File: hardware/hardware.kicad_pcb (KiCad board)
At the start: 2 copper layers, 25.7 x 34.4 mm, 10 parts, among them P1 CONN_01X08, P2 CONN_01X08, P3 CONN_01X02

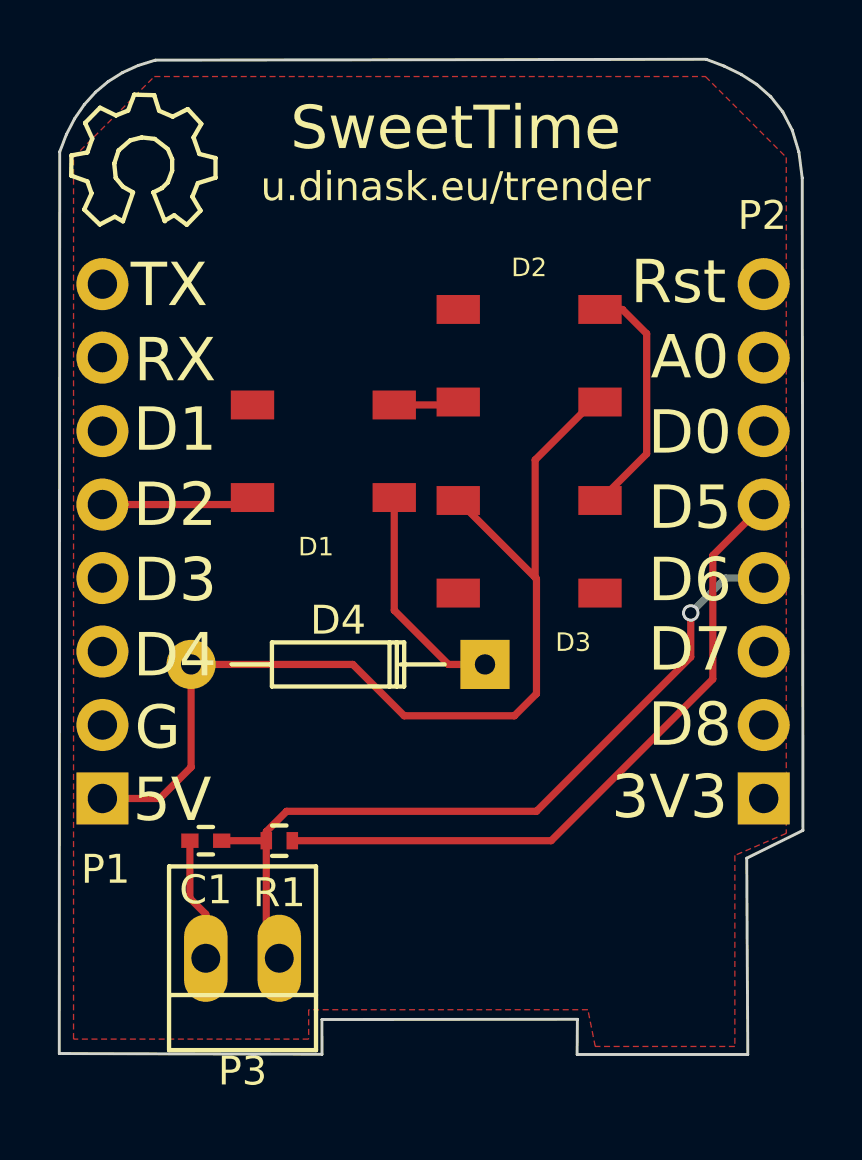
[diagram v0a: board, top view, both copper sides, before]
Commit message: 1st re-reading * serial resistor with DIN * decoupling capa for led power * D4 footprint
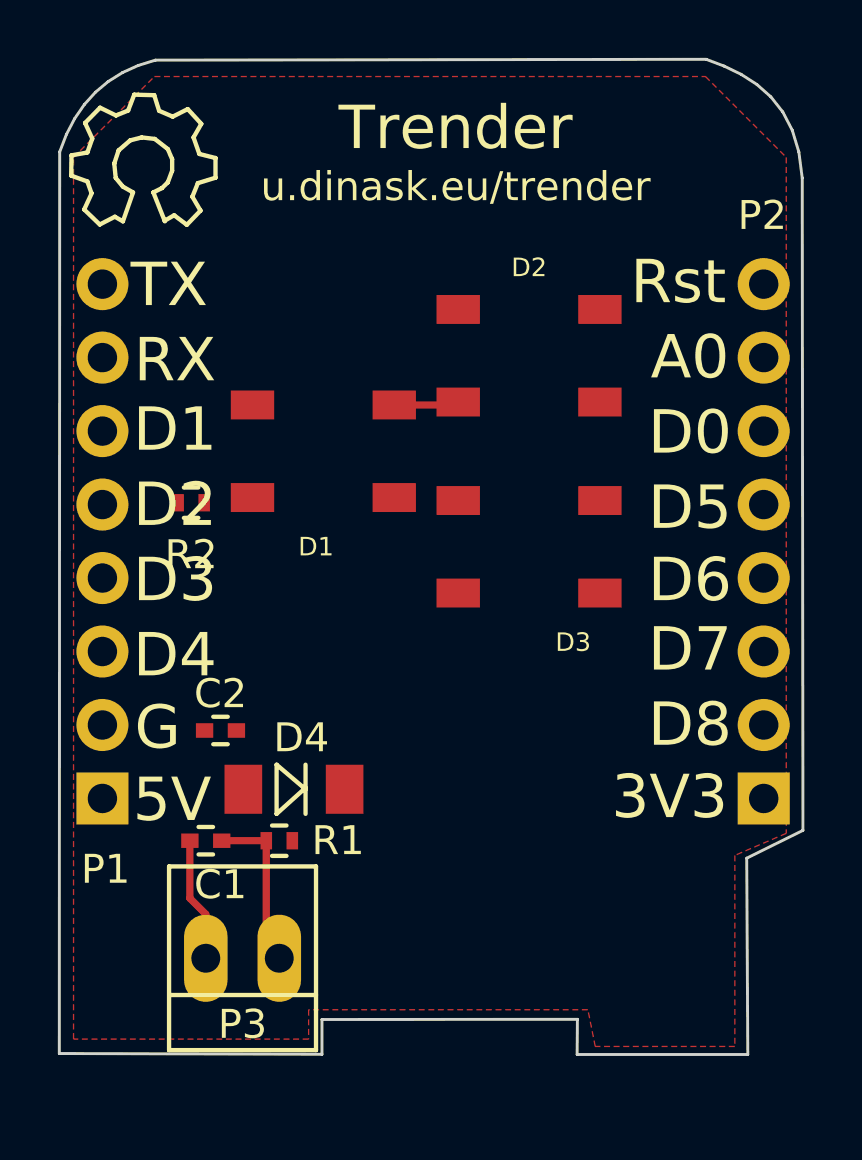
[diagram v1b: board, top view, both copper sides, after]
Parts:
- added C2: 4.7u, Capacitors_SMD:C_0402, F.Cu at (131.6, 101.6)
- added R2: 470, Resistors_SMD:R_0402, F.Cu at (130.6, 93.7)
- D4: value 1N4004 -> 1N4148; footprint Diodes_ThroughHole:Diode_DO-35_SOD27_Horizontal_RM10 -> Diodes_SMD:MiniMELF_Standard
- moved D4 7.89 mm to (134.1, 103.6)
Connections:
- D1 pad 4: /D2 -> Net-(D1-Pad4)
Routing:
- net /+5V: track 35.0 -> 0.24 mm
- net /D5: track 23.6 -> 0.00 mm
- net /D6: track 27.8 -> 5.79 mm, vias 1 -> 0
- net Net-(D2-Pad2): track 8.40 -> 0.00 mm
- net Net-(D1-Pad1): track 7.81 -> 0.00 mm
- net /D2: track 5.29 -> 0.00 mm
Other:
- board text added: "Trender"
- board text removed: "SweetTime"

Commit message: 1st review : placement/routage
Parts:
- moved C2 7.22 mm to (136.1, 96.0)
- moved D4 4.50 mm to (132.8, 99.3), turned to 270 degrees
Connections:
- C1 pad 1: /D6 -> /D5
- P3 pad 1: /D6 -> /D5
- R1 pad 1: /D5 -> /D6
- R1 pad 2: /D6 -> /D5
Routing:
- net /D5: track 0.00 -> 29.2 mm
- net /+5V: track 0.24 -> 24.0 mm
- net /D6: track 5.79 -> 20.1 mm
- net Net-(D2-Pad2): track 0.00 -> 7.74 mm
- net Net-(D1-Pad1): track 0.00 -> 6.85 mm
- net /D2: track 0.00 -> 2.64 mm
- net Net-(D1-Pad4): track 0.34 -> 2.09 mm
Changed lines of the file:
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@@
   (general
     (links 19)
-    (no_connects 11)
+    (no_connects 0)
     (area 125.949806 78.348265 151.756027 112.850001)
     (thickness 1.6)
     (drawings 75)
-    (tracks 11)
+    (tracks 44)
     (zones 0)
     (modules 12)
@@
     (34 B.Paste user)
     (35 F.Paste user)
-    (36 B.SilkS user)
+    (36 B.SilkS user hide)
     (37 F.SilkS user)
     (38 B.Mask user)
@@
     (fp_line (start -0.25 0.475) (end 0.25 0.475) (layer F.SilkS) (width 0.15))
     (pad 1 smd rect (at -0.55 0 180) (size 0.6 0.5) (layers F.Cu F.Paste F.Mask)
-      (net 11 /D6))
+      (net 12 /D5))
     (pad 2 smd rect (at 0.55 0 180) (size 0.6 0.5) (layers F.Cu F.Paste F.Mask)
       (net 16 GND))
@@
     (fp_line (start 2.54 -3.175) (end 2.54 3.175) (layer F.SilkS) (width 0.15))
     (pad 1 thru_hole oval (at -1.27 0 180) (size 1.50622 3.01498) (drill 0.99822) (layers *.Cu *.Mask)
-      (net 11 /D6))
+      (net 12 /D5))
     (pad 2 thru_hole oval (at 1.27 0 180) (size 1.50622 3.01498) (drill 0.99822) (layers *.Cu *.Mask)
       (net 16 GND))
@@
     (fp_line (start -0.25 0.525) (end 0.25 0.525) (layer F.SilkS) (width 0.15))
     (pad 1 smd rect (at -0.45 0 180) (size 0.4 0.6) (layers F.Cu F.Paste F.Mask)
+      (net 11 /D6))
+    (pad 2 smd rect (at 0.45 0 180) (size 0.4 0.6) (layers F.Cu F.Paste F.Mask)
       (net 12 /D5))
-    (pad 2 smd rect (at 0.45 0 180) (size 0.4 0.6) (layers F.Cu F.Paste F.Mask)
-      (net 11 /D6))
     (model Resistors_SMD.3dshapes/R_0402.wrl
       (at (xyz 0 0 0))
@@
   )
   (module Capacitors_SMD:C_0402 (layer F.Cu)
-    (at 131.572 101.6 180)
+    (at 136.144 96.012 180)
     (descr "Capacitor SMD 0402, reflow soldering, AVX (see smccp.pdf)")
     (tags "capacitor 0402")
     (attr smd)
-    (fp_text reference C2 (at 0 1.27 180) (layer F.SilkS)
+    (fp_text reference C2 (at 0 -1.27 180) (layer F.SilkS)
       (effects (font (size 1 1) (thickness 0.15)))
     )
@@
   )
   (module Diodes_SMD:MiniMELF_Standard (layer F.Cu)
-    (at 134.112 103.632 180)
+    (at 132.842 99.314 270)
     (descr "Diode Mini-MELF Standard")
     (tags "Diode Mini-MELF Standard")
     (attr smd)
-    (fp_text reference D4 (at -0.254 1.778 180) (layer F.SilkS)
-      (effects (font (size 1 1) (thickness 0.15)))
-    )
-    (fp_text value 1N4148 (at 0 3.81 180) (layer F.Fab) hide
+    (fp_text reference D4 (at 0 -1.778 270) (layer F.SilkS)
+      (effects (font (size 1 1) (thickness 0.15)))
+    )
+    (fp_text value 1N4148 (at 0 3.81 270) (layer F.Fab) hide
       (effects (font (size 1 1) (thickness 0.15)))
     )
@@
     (fp_line (start 0.60052 0.85) (end -0.40024 0) (layer F.SilkS) (width 0.15))
     (fp_line (start -0.40024 -0.85) (end -0.40024 0.85) (layer F.SilkS) (width 0.15))
-    (fp_text user K (at -1.8 1.95 180) (layer F.SilkS) hide
-      (effects (font (size 1 1) (thickness 0.15)))
-    )
-    (fp_text user A (at 1.8 1.95 180) (layer F.SilkS) hide
+    (fp_text user K (at -1.8 1.95 270) (layer F.SilkS) hide
+      (effects (font (size 1 1) (thickness 0.15)))
+    )
+    (fp_text user A (at 1.8 1.95 270) (layer F.SilkS) hide
       (effects (font (size 1 1) (thickness 0.15)))
     )
     (fp_circle (center 0 0) (end 0 0.55118) (layer F.Adhes) (width 0.381))
     (fp_circle (center 0 0) (end 0 0.20066) (layer F.Adhes) (width 0.381))
-    (pad 1 smd rect (at -1.75006 0 180) (size 1.30048 1.69926) (layers F.Cu F.Paste F.Mask)
+    (pad 1 smd rect (at -1.75006 0 270) (size 1.30048 1.69926) (layers F.Cu F.Paste F.Mask)
       (net 17 "Net-(D1-Pad1)"))
-    (pad 2 smd rect (at 1.75006 0 180) (size 1.30048 1.69926) (layers F.Cu F.Paste F.Mask)
+    (pad 2 smd rect (at 1.75006 0 270) (size 1.30048 1.69926) (layers F.Cu F.Paste F.Mask)
       (net 1 /+5V))
     (model Diodes_SMD.3dshapes/MiniMELF_Standard.wrl
@@
   (gr_line (start 143.9 112.8) (end 143.909849 111.583795) (layer Edge.Cuts) (width 0.1))
   (gr_line (start 149.8 112.8) (end 143.9 112.8) (layer Edge.Cuts) (width 0.1))
+  (segment (start 132.842 101.06406) (end 133.12394 101.06406) (width 0.25) (layer F.Cu) (net 1))
+  (segment (start 133.12394 101.06406) (end 136.694 97.494) (width 0.25) (layer F.Cu) (net 1))
+  (segment (start 136.694 97.494) (end 136.694 96.012) (width 0.25) (layer F.Cu) (net 1))
+  (segment (start 127.49 103.95) (end 129.95606 103.95) (width 0.25) (layer F.Cu) (net 1))
+  (segment (start 129.95606 103.95) (end 132.842 101.06406) (width 0.25) (layer F.Cu) (net 1))
+  (segment (start 136.694 96.012) (end 137.428 96.012) (width 0.25) (layer F.Cu) (net 1))
+  (segment (start 137.428 96.012) (end 139.79 93.65) (width 0.25) (layer F.Cu) (net 1))
+  (segment (start 139.79 93.65) (end 141.286 93.65) (width 0.25) (layer F.Cu) (net 1))
+  (segment (start 141.286 93.65) (end 144.69 90.246) (width 0.25) (layer F.Cu) (net 1))
   (segment (start 144.45 90.246) (end 144.69 90.246) (width 0.25) (layer F.Cu) (net 1))
-  (segment (start 133.154 105.41) (end 133.154 109.024) (width 0.25) (layer F.Cu) (net 11))
-  (segment (start 133.154 109.024) (end 133.604 109.474) (width 0.25) (layer F.Cu) (net 11))
-  (segment (start 131.614 105.41) (end 133.154 105.41) (width 0.25) (layer F.Cu) (net 11))
+  (segment (start 130.106 93.726) (end 127.554 93.726) (width 0.25) (layer F.Cu) (net 4))
+  (segment (start 127.554 93.726) (end 127.49 93.79) (width 0.25) (layer F.Cu) (net 4))
+  (segment (start 134.054 105.41) (end 139.7 105.41) (width 0.25) (layer F.Cu) (net 11))
+  (segment (start 148.78 96.33) (end 150.35 96.33) (width 0.25) (layer F.Cu) (net 11))
+  (segment (start 139.7 105.41) (end 148.78 96.33) (width 0.25) (layer F.Cu) (net 11))
+  (segment (start 133.154 105.41) (end 133.154 104.844) (width 0.25) (layer F.Cu) (net 12))
+  (segment (start 148.272 93.79) (end 150.35 93.79) (width 0.25) (layer F.Cu) (net 12))
+  (segment (start 147.066 94.996) (end 148.272 93.79) (width 0.25) (layer F.Cu) (net 12))
+  (segment (start 147.066 96.774) (end 147.066 94.996) (width 0.25) (layer F.Cu) (net 12))
+  (segment (start 139.446 104.394) (end 147.066 96.774) (width 0.25) (layer F.Cu) (net 12))
+  (segment (start 133.604 104.394) (end 139.446 104.394) (width 0.25) (layer F.Cu) (net 12))
+  (segment (start 133.154 104.844) (end 133.604 104.394) (width 0.25) (layer F.Cu) (net 12))
+  (segment (start 133.154 105.41) (end 133.154 109.024) (width 0.25) (layer F.Cu) (net 12))
+  (segment (start 133.154 109.024) (end 133.604 109.474) (width 0.25) (layer F.Cu) (net 12))
+  (segment (start 131.614 105.41) (end 133.154 105.41) (width 0.25) (layer F.Cu) (net 12))
   (segment (start 127.49 101.41) (end 127.952 101.41) (width 0.25) (layer F.Cu) (net 16))
   (segment (start 131.064 109.474) (end 131.064 107.95) (width 0.25) (layer F.Cu) (net 16))
   (segment (start 130.514 107.4) (end 130.514 105.41) (width 0.25) (layer F.Cu) (net 16))
   (segment (start 131.064 107.95) (end 130.514 107.4) (width 0.25) (layer F.Cu) (net 16))
+  (segment (start 132.842 97.56394) (end 133.06806 97.56394) (width 0.25) (layer F.Cu) (net 17))
+  (segment (start 133.06806 97.56394) (end 134.62 96.012) (width 0.25) (layer F.Cu) (net 17))
+  (segment (start 134.62 96.012) (end 134.62 95.25) (width 0.25) (layer F.Cu) (net 17))
+  (segment (start 134.62 95.25) (end 135.128 94.742) (width 0.25) (layer F.Cu) (net 17))
+  (segment (start 135.128 94.742) (end 136.384 94.742) (width 0.25) (layer F.Cu) (net 17))
+  (segment (start 136.384 94.742) (end 137.578 93.548) (width 0.25) (layer F.Cu) (net 17))
   (segment (start 137.578 90.348) (end 139.688 90.348) (width 0.25) (layer F.Cu) (net 18))
   (segment (start 139.688 90.348) (end 139.79 90.246) (width 0.25) (layer F.Cu) (net 18))
+  (segment (start 144.69 87.046) (end 144.704 87.046) (width 0.25) (layer F.Cu) (net 19))
+  (segment (start 144.704 87.046) (end 146.05 88.392) (width 0.25) (layer F.Cu) (net 19))
+  (segment (start 146.05 88.392) (end 146.05 92.29) (width 0.25) (layer F.Cu) (net 19))
+  (segment (start 146.05 92.29) (end 144.69 93.65) (width 0.25) (layer F.Cu) (net 19))
+  (segment (start 131.006 93.726) (end 132.5 93.726) (width 0.25) (layer F.Cu) (net 21))
+  (segment (start 132.5 93.726) (end 132.678 93.548) (width 0.25) (layer F.Cu) (net 21))
   (segment (start 132.436 93.79) (end 132.678 93.548) (width 0.25) (layer F.Cu) (net 21))
   (zone (net 16) (net_name GND) (layer F.Cu) (hatch edge 0.508)

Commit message: Move button input to 3.3V
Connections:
- R1 pad 1: /D6 -> /+3.3V
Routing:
- net /D6: track 20.1 -> 0.00 mm
- net /+3.3V: track 0.00 -> 16.9 mm
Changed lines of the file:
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@@
     (fp_line (start -0.25 0.525) (end 0.25 0.525) (layer F.SilkS) (width 0.15))
     (pad 1 smd rect (at -0.45 0 180) (size 0.4 0.6) (layers F.Cu F.Paste F.Mask)
-      (net 11 /D6))
+      (net 8 /+3.3V))
     (pad 2 smd rect (at 0.45 0 180) (size 0.4 0.6) (layers F.Cu F.Paste F.Mask)
       (net 12 /D5))
@@
   (segment (start 130.106 93.726) (end 127.554 93.726) (width 0.25) (layer F.Cu) (net 4))
   (segment (start 127.554 93.726) (end 127.49 93.79) (width 0.25) (layer F.Cu) (net 4))
-  (segment (start 134.054 105.41) (end 139.7 105.41) (width 0.25) (layer F.Cu) (net 11))
-  (segment (start 148.78 96.33) (end 150.35 96.33) (width 0.25) (layer F.Cu) (net 11))
-  (segment (start 139.7 105.41) (end 148.78 96.33) (width 0.25) (layer F.Cu) (net 11))
+  (segment (start 134.054 105.41) (end 140.208 105.41) (width 0.25) (layer F.Cu) (net 8) (status 400000))
+  (segment (start 141.668 103.95) (end 150.35 103.95) (width 0.25) (layer F.Cu) (net 8) (status 800000))
+  (segment (start 140.208 105.41) (end 141.668 103.95) (width 0.25) (layer F.Cu) (net 8))
   (segment (start 133.154 105.41) (end 133.154 104.844) (width 0.25) (layer F.Cu) (net 12))
   (segment (start 148.272 93.79) (end 150.35 93.79) (width 0.25) (layer F.Cu) (net 12))

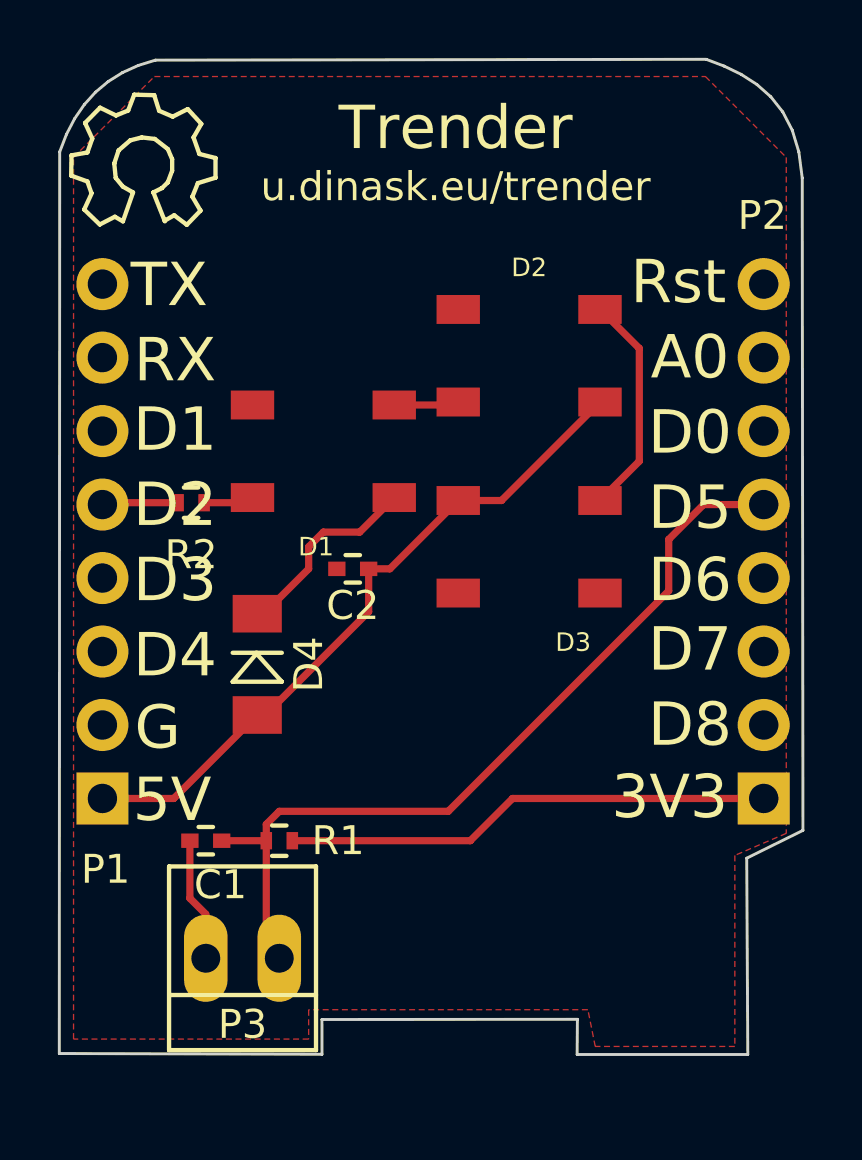
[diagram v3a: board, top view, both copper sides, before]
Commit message: Add connector for led extensions
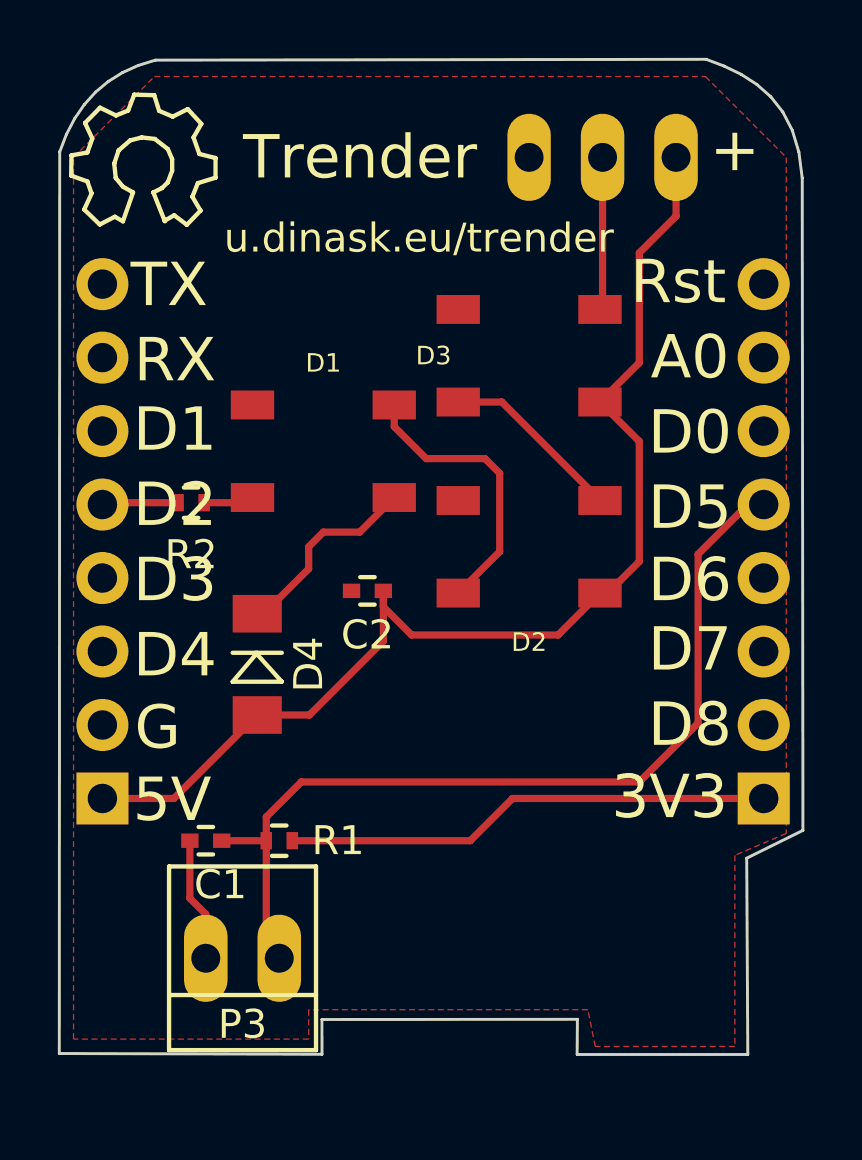
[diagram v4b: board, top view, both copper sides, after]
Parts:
- added P4: CONN_01X03, Connect:PINHEAD1-3, B.Cu at (144.8, 81.8)
- moved D2 6.60 mm to (142.2, 95.2)
- moved D3 6.60 mm to (142.2, 88.6), turned to 180 degrees
- moved C2 0.92 mm to (136.7, 96.8)
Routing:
- net /+5V: track 24.0 -> 41.0 mm
- net Net-(D1-Pad2): track 2.25 -> 9.80 mm
- net Net-(D3-Pad2): track 0.00 -> 5.30 mm
- net /D5: track 29.2 -> 31.7 mm
- net Net-(D2-Pad2): track 7.74 -> 6.32 mm
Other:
- board text added: "+"
